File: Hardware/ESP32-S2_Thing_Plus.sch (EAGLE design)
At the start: 64 parts, among them J3 QWIIC_RA, J5 USB-C, J6 JTAG, Q1 2.5A/30V, Q2 MBT3904DW1T1, U1 ESP32-S2-WROOM, U2 CP210X, U3 AP2112K-3.3V, U4 MCP73831, U5 TC7USB40MU, Y1 32.768kHz

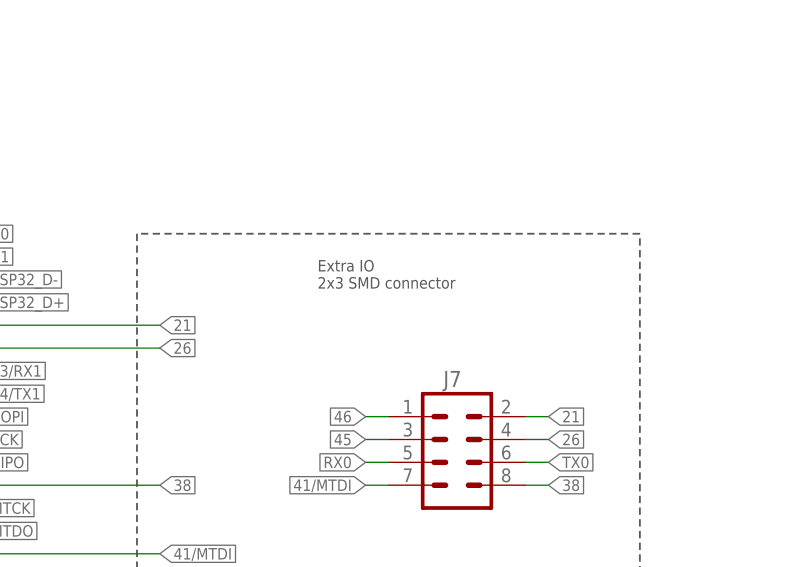
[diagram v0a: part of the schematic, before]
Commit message: corrected extra IO sch note, moved "0" button to align with reset.
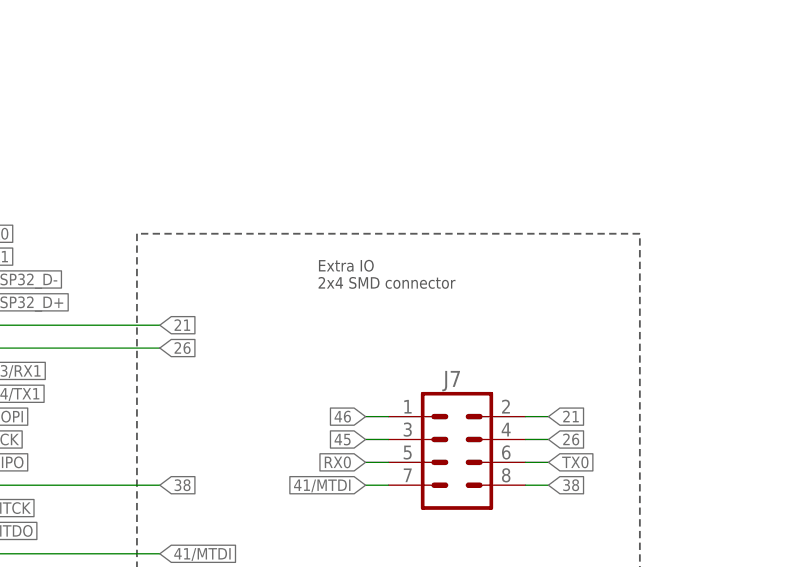
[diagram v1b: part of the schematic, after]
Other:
- note added: "Extra IO 2x4 SMD connector"
- note removed: "Extra IO 2x3 SMD connector"
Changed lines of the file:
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@@
 <wire x1="208.28" y1="88.9" x2="208.28" y2="142.24" width="0.2032" layer="97" style="shortdash"/>
 <text x="172.466" y="136.144" size="1.27" layer="97" font="vector">Extra IO
-2x3 SMD connector</text>
+2x4 SMD connector</text>
 <wire x1="198.12" y1="55.88" x2="121.92" y2="55.88" width="0.2032" layer="97" style="longdash"/>
 <wire x1="121.92" y1="55.88" x2="121.92" y2="0" width="0.2032" layer="97" style="longdash"/>

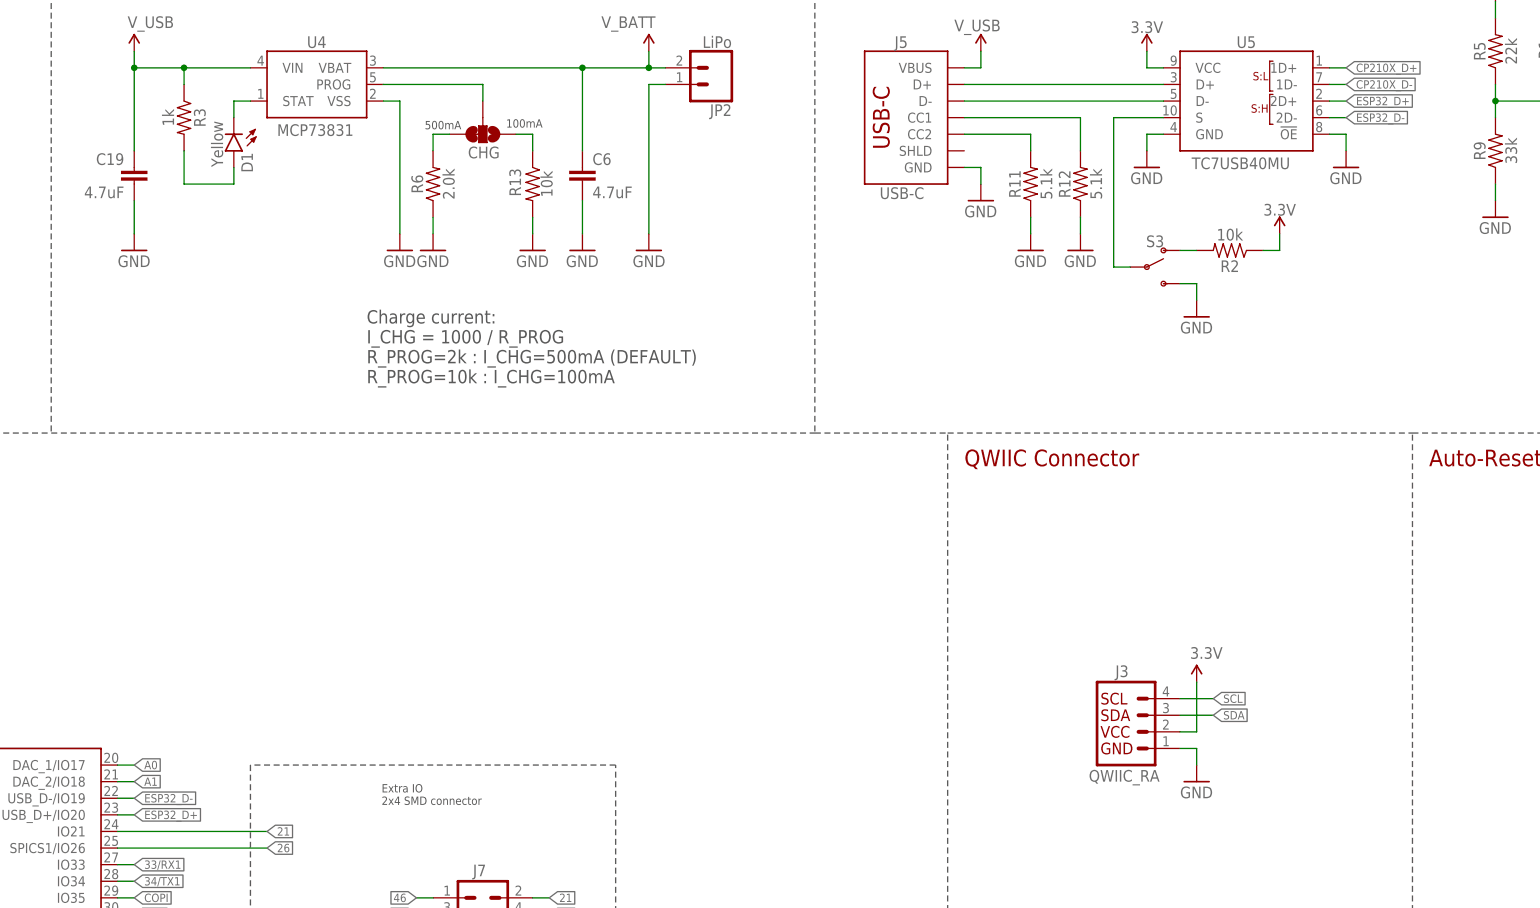
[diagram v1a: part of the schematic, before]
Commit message: Group design review changes - USB switch to jumper and much more!
-Moved USB selection switch to a 3-way jumper on the bottom.
-Increased Battery + and - label text size
-switched 5.1K resistors to 0402 package
-Moved Charge LED away from standoff
-More GND vias under CP210X
-More GND vias near GND pad on JST batt input
-added pullup on GPIO18 as recommended in datasheet. connected with a NC trace jumper, so user can easily remove if they want. Added big text warning about it in sch.
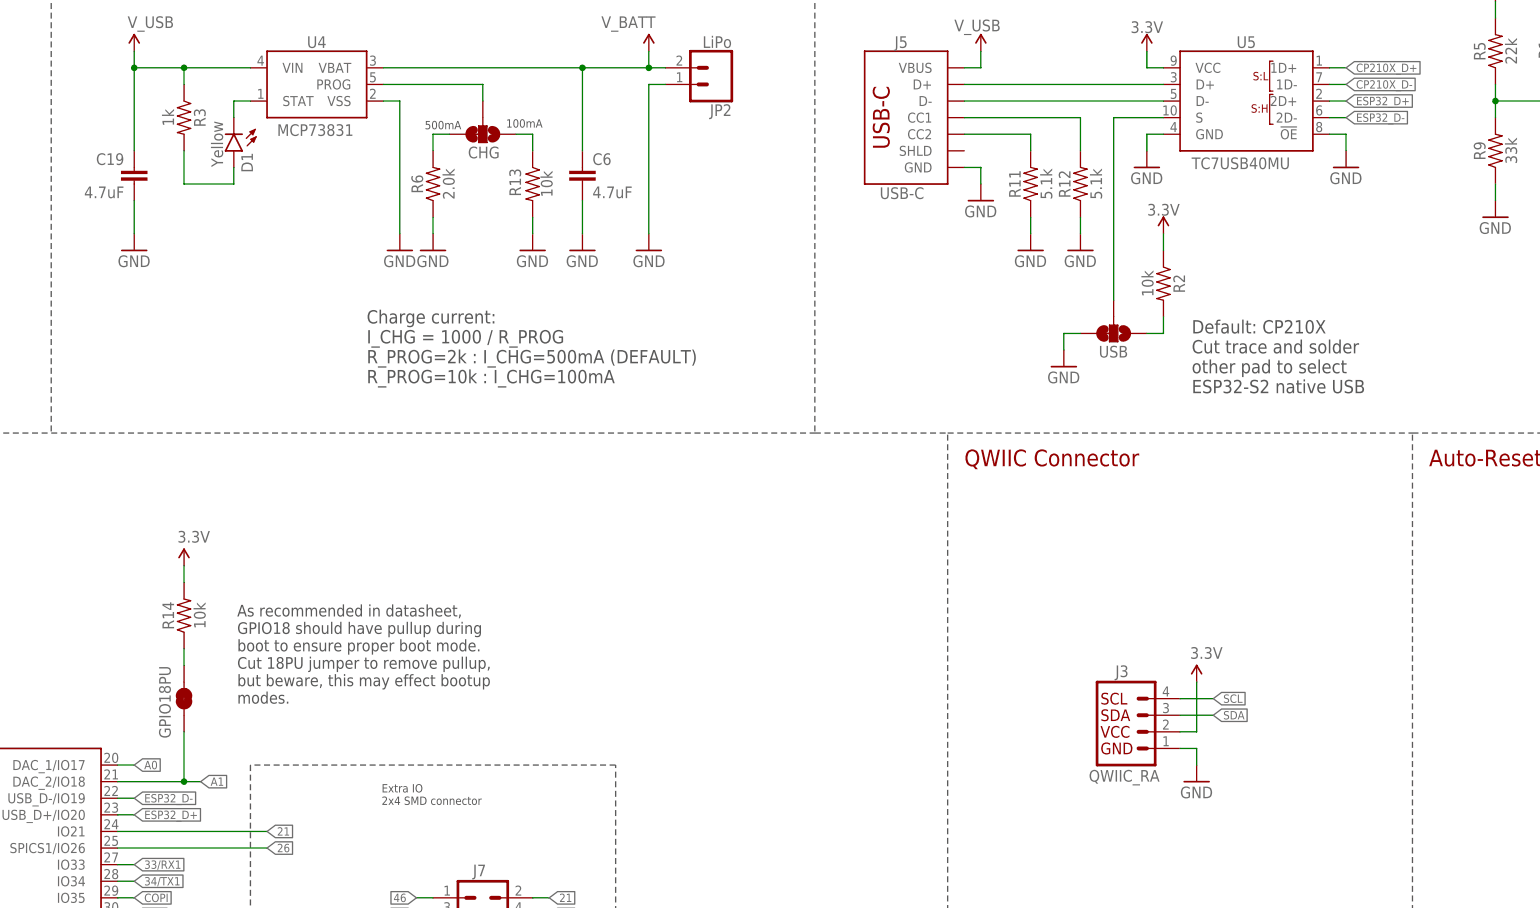
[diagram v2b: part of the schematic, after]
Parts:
- removed S3: (no value), SparkFun-Switches:SWITCH-SPDT-SMD-RIGHT-ANGLE
- added GPIO18PU: JUMPER-SMT_2_NC_TRACE_SILK, SparkFun-Jumpers:JUMPER-SMT_2_NC_TRACE_SILK
- added R14: 10k, SparkFun-Resistors:10KOHM-0402T-1/16W-1%
- added USB: JUMPER-SMT_3_1-NC_TRACE_SILK, SparkFun-Jumpers:JUMPER-SMT_3_1-NC_TRACE_SILK
- R11, R12: device SparkFun-Resistors:5.1KOHM5.1KOHM-0603-1/10W-1% -> SparkFun-Resistors:5.1KOHM-0402T-1/16W-1%
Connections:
- new net N$14: GPIO18PU.2, R14.1
- net 3.3V: now also R14.2
- net A1: now also GPIO18PU.1
- net GND: now also USB.3; no longer S3.S
- net N$6: now also USB.1; no longer S3.O
- net USB_SEL: now also USB.2; no longer S3.P
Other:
- note added: "As recommended in datasheet, GPIO18 should have pullup during boot to ensure proper boot mode. Cut 18PU jumper to remove pullup, but beware, this may effect bootup modes."
- note added: "Default: CP210X Cut trace and solder other pad to select ESP32-S2 native USB"
- moved on the sheet: R2

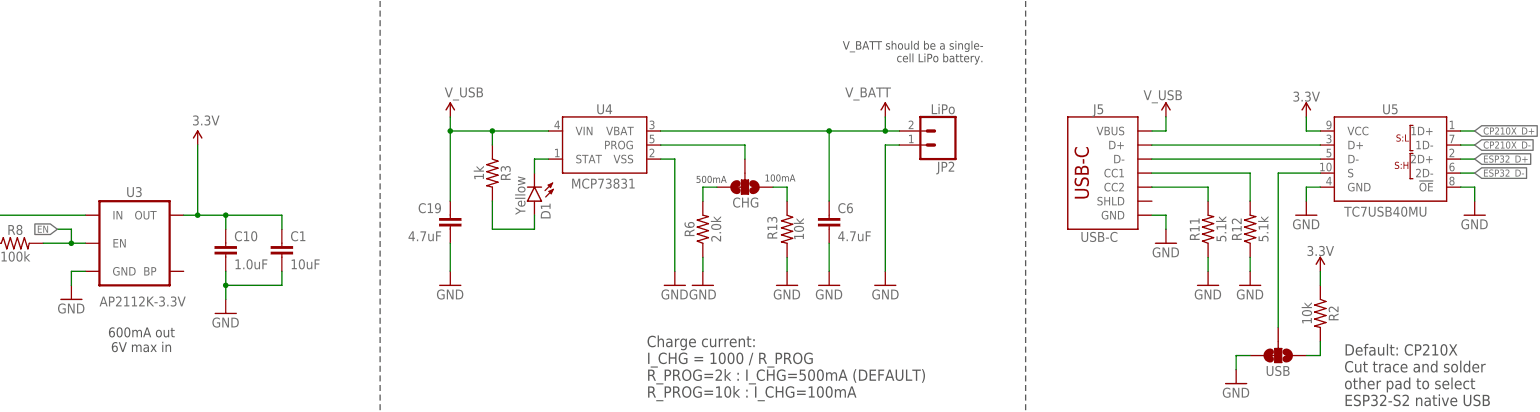
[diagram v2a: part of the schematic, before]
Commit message: Final changes from groupd proto review (library work)
-Added tNames and tValues to TC7 USB switch IC.
-repositioned tNames and tValues on CP210X footprint.
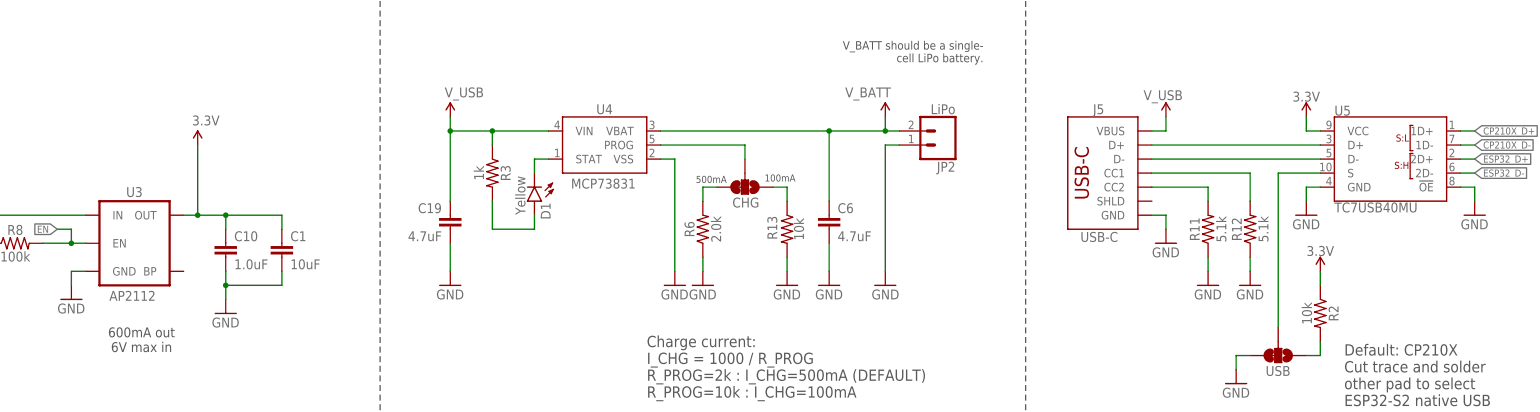
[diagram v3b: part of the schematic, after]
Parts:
- U3: value AP2112K-3.3V -> AP2112

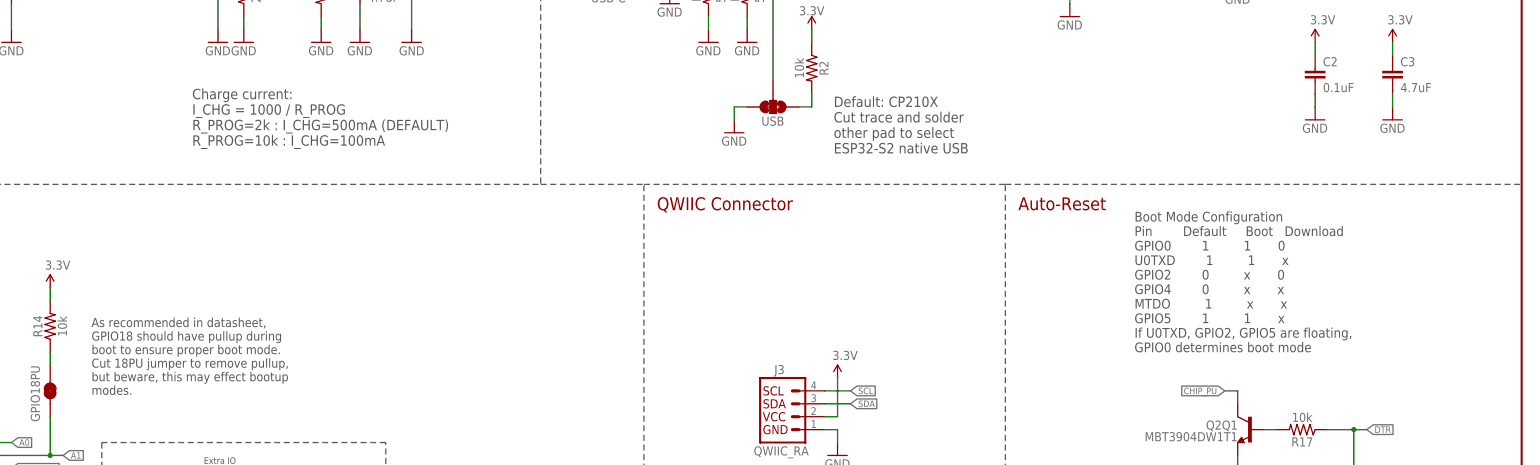
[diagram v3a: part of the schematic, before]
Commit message: eng run checklist
-one proportional font in sch fixed.
-updated auto-reset paragraph in sch to reflect S2 strapping pins
-updated USB selection jumper paragraph to more clearly show options and default.
-removed S2 Module dimensions from footprint (forgot about them while doing the library work early on)
-added more dimensions for header rows
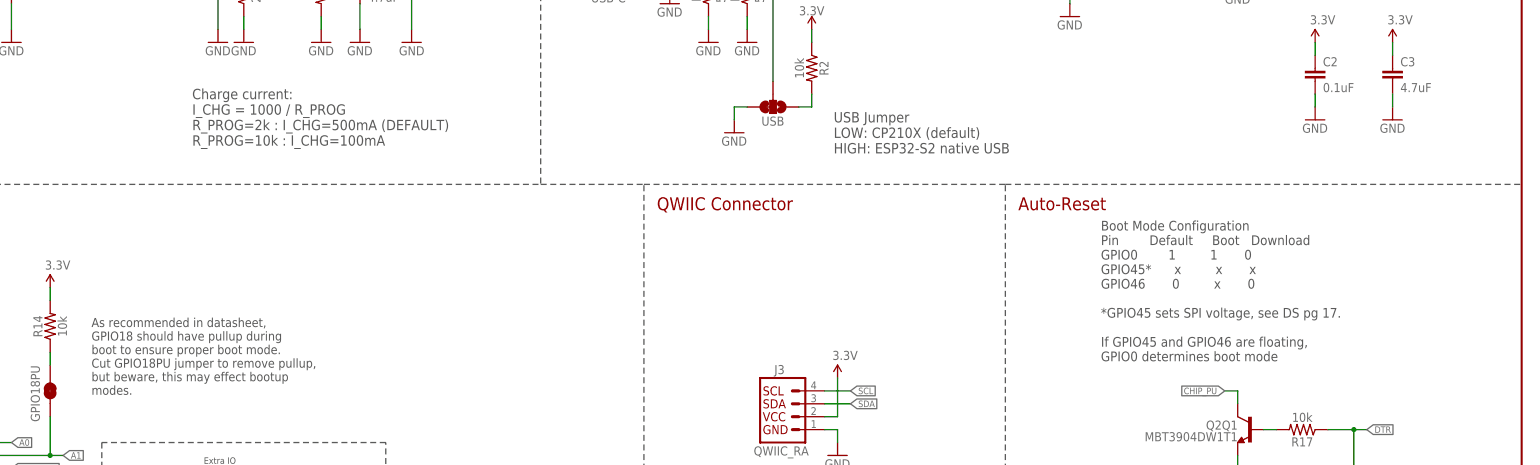
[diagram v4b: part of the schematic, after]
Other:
- note added: "As recommended in datasheet, GPIO18 should have pullup during boot to ensure proper boot mode. Cut GPIO18PU jumper to remove pullup, but beware, this may effect bootup modes."
- note added: "Boot Mode Configuration Pin Default Boot Download GPIO0 1 1 0 GPIO45* x x x GPIO46 0 x 0 *GPIO45 sets SPI voltage, see DS pg 17. If GPIO45 and GPIO46 are floating, GPIO0 determines boot mode"
- note added: "USB Jumper LOW: CP210X (default) HIGH: ESP32-S2 native USB"
- note removed: "As recommended in datasheet, GPIO18 should have pullup during boot to ensure proper boot mode. Cut 18PU jumper to remove pullup, but beware, this may effect bootup modes."
- note removed: "Boot Mode Configuration Pin Default Boot Download GPIO0 1 1 0 U0TXD 1 1 x GPIO2 0 x 0 GPIO4 0 x x MTDO 1 x x GPIO5 1 1 x If U0TXD, GPIO2, GPIO5 are floating, GPIO0 determines boot mode"
- note removed: "Default: CP210X Cut trace and solder other pad to select ESP32-S2 native USB"
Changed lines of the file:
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@@
 <sheet>
 <plain>
-<text x="355.6" y="160.02" size="1.905" layer="97" font="vector">Boot Mode Configuration
+<text x="348.996" y="158.242" size="1.905" layer="97" font="vector">Boot Mode Configuration
 Pin        Default     Boot   Download
 GPIO0        1         1       0
-U0TXD        1         1       x
-GPIO2        0         x       0
-GPIO4        0         x       x
-MTDO         1         x       x
-GPIO5        1         1       x
-If U0TXD, GPIO2, GPIO5 are floating,
+GPIO45*      x         x       x
+GPIO46       0         x       0
+*GPIO45 sets SPI voltage, see DS pg 17.
+If GPIO45 and GPIO46 are floating,
 GPIO0 determines boot mode</text>
 <text x="243.84" y="274.32" size="2.54" layer="94" font="vector">CP2104/2N (USB-to-Serial Converter)</text>
@@
 <text x="126.238" y="50.038" size="2.54" layer="94" font="vector">JTAG</text>
 <text x="4.572" y="184.15" size="1.778" layer="97" font="vector">Module recommended VCC range: 3.0-3.6V</text>
-<text x="296.418" y="199.136" size="2.032" layer="97" font="vector" rot="MR180" align="top-left">Default: CP210X
-Cut trace and solder
-other pad to select
-ESP32-S2 native USB</text>
-<text x="150.368" y="151.638" size="1.778" layer="97">As recommended in datasheet,
+<text x="296.418" y="199.136" size="2.032" layer="97" font="vector" rot="MR180" align="top-left">USB Jumper
+LOW: CP210X (default)
+HIGH: ESP32-S2 native USB</text>
+<text x="150.368" y="151.638" size="1.778" layer="97" font="vector">As recommended in datasheet,
 GPIO18 should have pullup during
 boot to ensure proper boot mode.
-Cut 18PU jumper to remove pullup,
+Cut GPIO18PU jumper to remove pullup,
 but beware, this may effect bootup
 modes.</text>
